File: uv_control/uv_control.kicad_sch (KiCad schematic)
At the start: 28 parts, among them J1 Keypad, J2 Safety Led, J3 Safety, J4 Fan, J5 12V Power, J6 Safety Led, J7 Light Power, Q1 BSS138, Q2 BSS138, Q3 IRFS7730-7, U1 MCP1415, U2 L7805

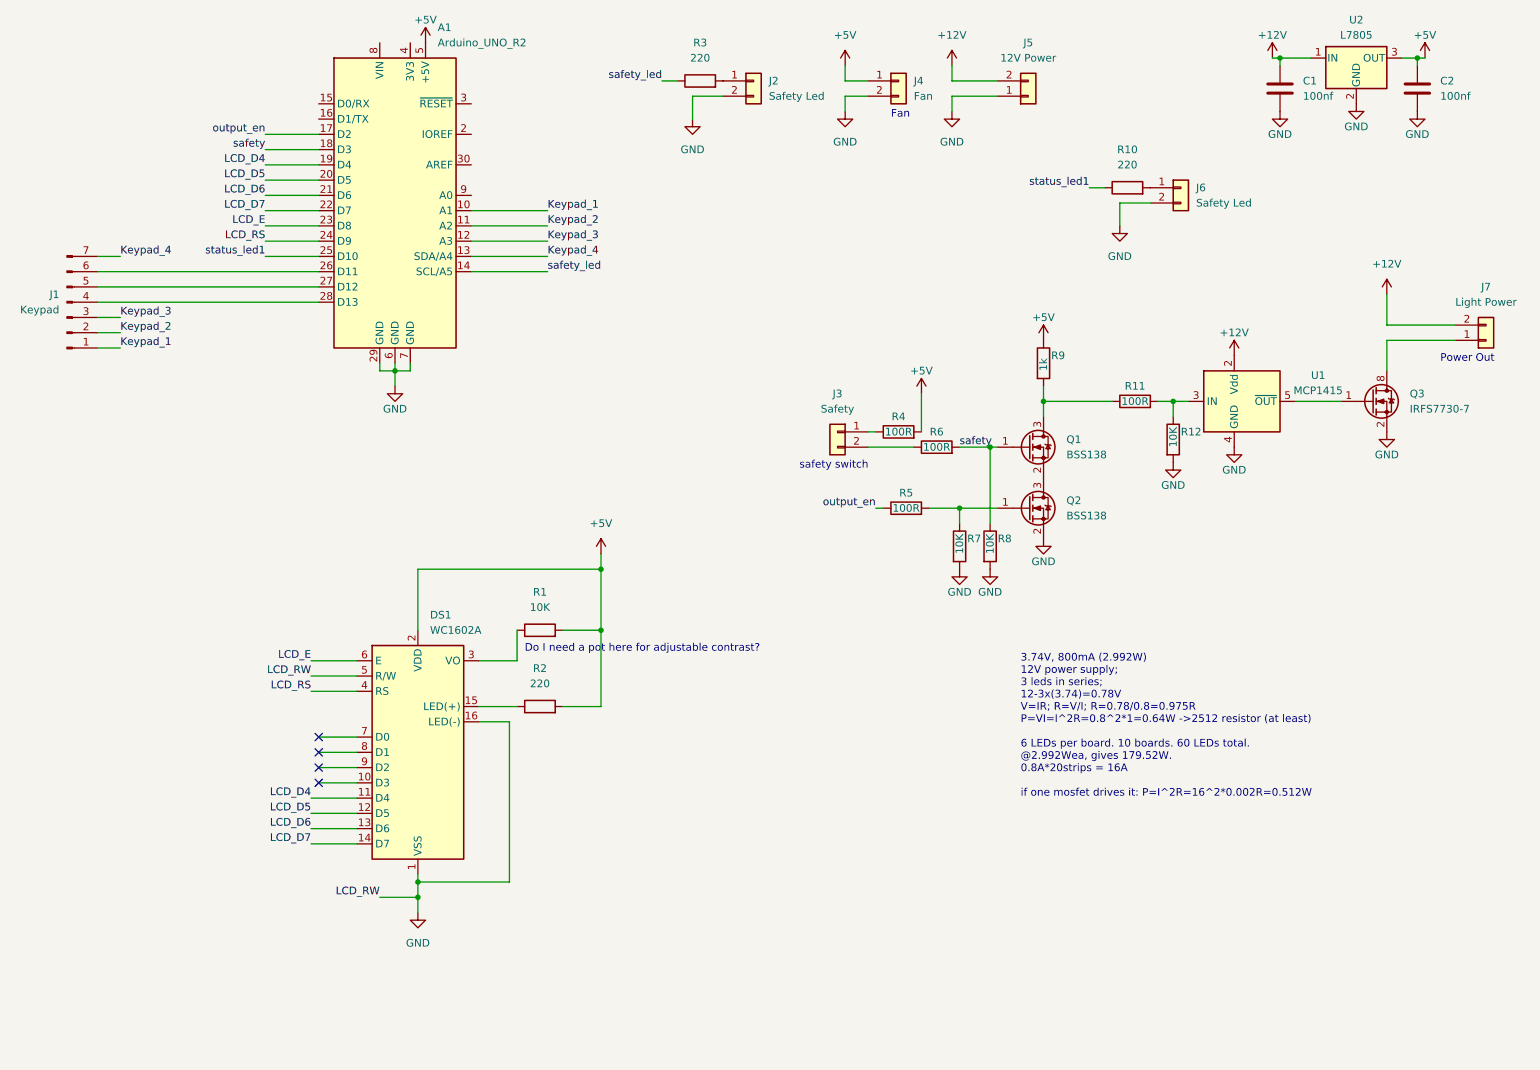
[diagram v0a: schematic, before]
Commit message: Changing v2 to a RP2040 based solution
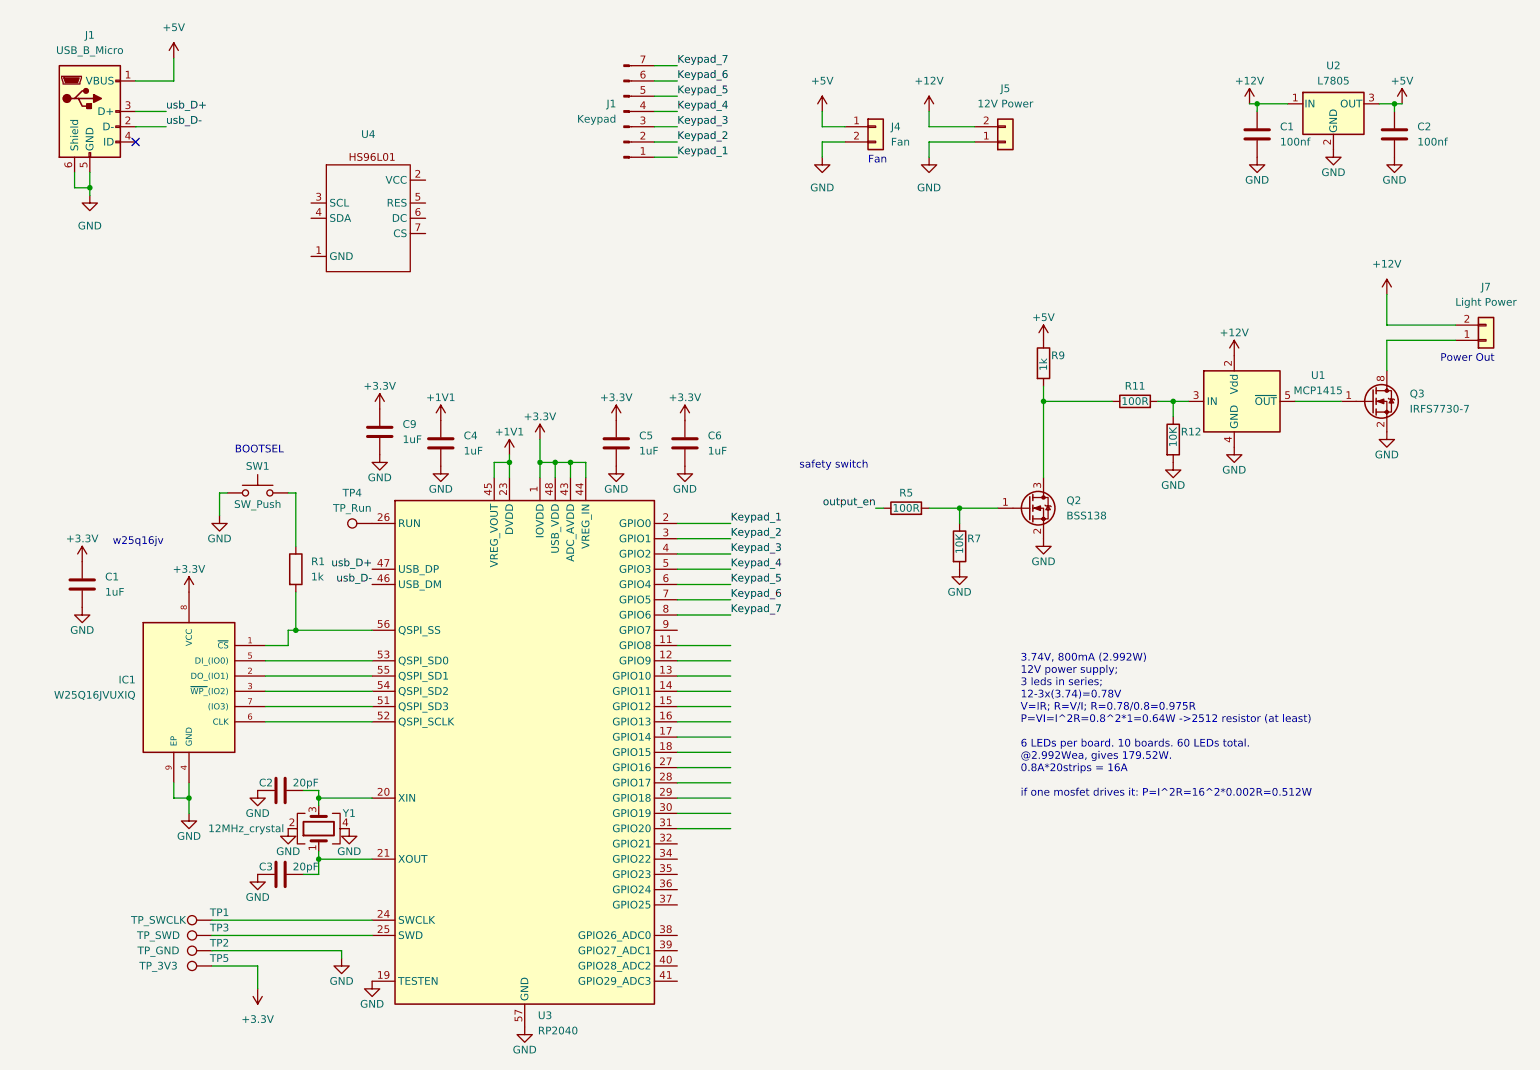
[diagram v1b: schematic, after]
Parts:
- removed A1: Arduino_UNO_R2, Module:Arduino_UNO_R2, symbol MCU_Module:Arduino_UNO_R2
- removed DS1: WC1602A, Display:WC1602A, symbol Display_Character:WC1602A
- removed J2, J6: Safety Led, Connector_JST:JST_EH_B2B-EH-A_1x02_P2.50mm_Vertical, symbol Connector_Generic:Conn_01x02
- removed J3: Safety, Connector_JST:JST_EH_B2B-EH-A_1x02_P2.50mm_Vertical, symbol Connector_Generic:Conn_01x02
- removed Q1: BSS138, Package_TO_SOT_SMD:SOT-23, symbol Transistor_FET:BSS138
- removed R10, R2, R3: 220, Resistor_SMD:R_0805_2012Metric_Pad1.20x1.40mm_HandSolder, symbol Device:R
- removed R4, R6: 100R, Resistor_SMD:R_0805_2012Metric, symbol Device:R
- removed R8: 10K, Resistor_SMD:R_0805_2012Metric, symbol Device:R
- added C1, C4, C5, C6, C9: 1uF, Capacitor_SMD:C_0402_1005Metric, symbol Device:C
- added C2, C3: 20pF, Capacitor_SMD:C_0402_1005Metric, symbol Device:C
- added IC1: W25Q16JVUXIQ, DIY_Watch_lib:SON50P300X200X60-9N, symbol DIY_Watch_lib:W25Q16JVUXIQ
- added J1: USB_B_Micro, Connector_USB:USB_Micro-B_GCT_USB3076-30-A, symbol Connector:USB_B_Micro
- added SW1: SW_Push, Button_Switch_SMD:SW_SPST_EVQP7C, symbol Switch:SW_Push
- added TP1: TP_SWCLK, TestPoint:TestPoint_Pad_D1.5mm, symbol Connector:TestPoint
- added TP2: TP_GND, TestPoint:TestPoint_Pad_D1.5mm, symbol Connector:TestPoint
- added TP3: TP_SWD, TestPoint:TestPoint_Pad_D1.5mm, symbol Connector:TestPoint
- added TP4: TP_Run, TestPoint:TestPoint_Pad_D1.0mm, symbol Connector:TestPoint
- added TP5: TP_3V3, TestPoint:TestPoint_Pad_D1.5mm, symbol Connector:TestPoint
- added U3: RP2040, Package_DFN_QFN:QFN-56-1EP_7x7mm_P0.4mm_EP3.2x3.2mm, symbol MCU_RaspberryPi:RP2040
- added U4: ~, uc_control:HS96L01, symbol uv_control:HS96L01
- added Y1: 12MHz_crystal, Crystal:Crystal_SMD_3225-4Pin_3.2x2.5mm, symbol Device:Crystal_GND24
- R1: value 10K -> 1k; footprint Resistor_SMD:R_0805_2012Metric_Pad1.20x1.40mm_HandSolder -> Resistor_SMD:R_0402_1005Metric
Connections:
- net +5V: now also J1.1 (VBUS); no longer R1.2
- net GND: now also C1.2, C2.1, C3.1, C4.2, C5.2, C6.2, C9.2, IC1.4 (GND), IC1.9 (EP), J1.5 (GND), J1.6 (Shield), SW1.1, TP2.1, U3.19 (TESTEN), U3.57 (GND), Y1.2, Y1.4
- net Keypad_1: now also U3.2 (GPIO0)
- net Keypad_2: now also U3.3 (GPIO1)
- net Keypad_3: now also U3.4 (GPIO2)
- net Keypad_4: now also J1.4 (Pin_4), U3.5 (GPIO3); no longer J1.7 (Pin_7)
- net at R11.1, R9.2: now also Q2.3 (D)
- net Keypad_5: now reaches J1.5 (Pin_5)
- net Keypad_5: now also U3.6 (GPIO4)
- net Keypad_6: now reaches J1.6 (Pin_6)
- net Keypad_6: now also U3.7 (GPIO5)
- net at R1.1: now also SW1.2
- new net: TP4.1, U3.26 (RUN)
- new net: TP3.1, U3.25 (SWD)
- new net: IC1.1 (~{CS}), R1.2, U3.56 (QSPI_SS)
- new net: C3.2, U3.21 (XOUT), Y1.1
- new net: C2.2, U3.20 (XIN), Y1.3
- new net: TP1.1, U3.24 (SWCLK)
- new net: IC1.2 (DO_(IO1)), U3.55 (QSPI_SD1)
- new net: IC1.3 (~{WP_}(IO2)), U3.54 (QSPI_SD2)
- new net: IC1.5 (DI_(IO0)), U3.53 (QSPI_SD0)
- new net: IC1.6 (CLK), U3.52 (QSPI_SCLK)
- new net: IC1.7 ((IO3)), U3.51 (QSPI_SD3)
- new net +1V1: C4.1, U3.23 (DVDD), U3.45 (VREG_VOUT), U3.50 (DVDD)
- new net +3.3V: C1.1, C5.1, C6.1, C9.1, IC1.8 (VCC), TP5.1, U3.1 (IOVDD), U3.10 (IOVDD), U3.22 (IOVDD), U3.33 (IOVDD), U3.42 (IOVDD), U3.43 (ADC_AVDD), U3.44 (VREG_IN), U3.48 (USB_VDD), U3.49 (IOVDD)
- new net Keypad_7: J1.7 (Pin_7), U3.8 (GPIO6)
- new net usb_D+: J1.3 (D+), U3.47 (USB_DP)
- new net usb_D-: J1.2 (D-), U3.46 (USB_DM)
- no-connect marks 4 -> 1
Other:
- note added: "BOOTSEL"
- note added: "w25q16jv"
- note removed: "Do I need a pot here for adjustable contrast?"
- moved on the sheet: C1, C2, J1, J4, J5, U2
